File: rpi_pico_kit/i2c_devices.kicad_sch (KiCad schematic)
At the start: 6 parts, among them J10 OLED Display SSD1306, J11 Conn_01x04_Male, J12 Conn_01x04_Male, U8 AT24CS32

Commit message: changed footprints from 0805 to 0603
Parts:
- C28: footprint Capacitor_SMD:C_0805_2012Metric_Pad1.18x1.45mm_HandSolder -> Capacitor_SMD:C_0603_1608Metric_Pad1.08x0.95mm_HandSolder; Supplier Part URL https://www.digikey.cz/en/products/detail/kemet/C0805C104M3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 -> (none)
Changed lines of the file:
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@@
       (effects (font (size 1.27 1.27)))
     )
-    (property "Footprint" "Capacitor_SMD:C_0805_2012Metric_Pad1.18x1.45mm_HandSolder" (id 2) (at 231.14 82.8548 0)
+    (property "Footprint" "Capacitor_SMD:C_0603_1608Metric_Pad1.08x0.95mm_HandSolder" (id 2) (at 231.14 82.8548 0)
       (effects (font (size 1.27 1.27)) hide)
     )
@@
       (effects (font (size 1.27 1.27)) hide)
     )
-    (property "Supplier Part URL" "https://www.digikey.cz/en/products/detail/kemet/C0805C104M3RAC7800/2211748" (id 6) (at 227.33 83.82 0)
+    (property "Supplier Part URL" "" (id 6) (at 227.33 83.82 0)
       (effects (font (size 1.27 1.27)) hide)
     )

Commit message: changed footprints for resistor arrays
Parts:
- RN8: footprint Resistor_SMD:R_Array_Convex_4x1206 -> Resistor_SMD:R_Array_Convex_4x0603
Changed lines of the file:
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@@
       (effects (font (size 1.27 1.27)) (justify right))
     )
-    (property "Footprint" "Resistor_SMD:R_Array_Convex_4x1206" (id 2) (at 97.282 68.58 90)
+    (property "Footprint" "Resistor_SMD:R_Array_Convex_4x0603" (id 2) (at 97.282 68.58 90)
       (effects (font (size 1.27 1.27)) hide)
     )
@@
       (effects (font (size 1.27 1.27)) (justify right))
     )
-    (property "Footprint" "Resistor_SMD:R_Array_Convex_4x1206" (id 2) (at 59.182 68.58 90)
+    (property "Footprint" "Resistor_SMD:R_Array_Convex_4x0603" (id 2) (at 59.182 68.58 90)
       (effects (font (size 1.27 1.27)) hide)
     )
@@
       (effects (font (size 1.27 1.27)) (justify right))
     )
-    (property "Footprint" "Resistor_SMD:R_Array_Convex_4x1206" (id 2) (at 106.172 68.58 90)
+    (property "Footprint" "Resistor_SMD:R_Array_Convex_4x0603" (id 2) (at 106.172 68.58 90)
       (effects (font (size 1.27 1.27)) hide)
     )
@@
       (effects (font (size 1.27 1.27)) (justify right))
     )
-    (property "Footprint" "Resistor_SMD:R_Array_Convex_4x1206" (id 2) (at 68.072 68.58 90)
-      (effects (font (size 1.27 1.27)) hide)
-    )
+    (property "Footprint" "Resistor_SMD:R_Array_Convex_4x0603" (id 2) (at 68.072 68.58 90)
+      (effects (font (size 1.27 1.27)) hide)
+    )

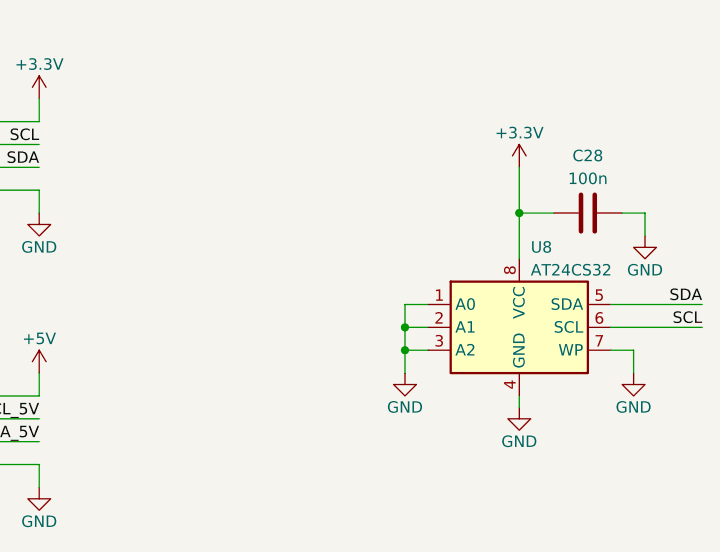
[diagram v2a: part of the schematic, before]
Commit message: changed eeprom I2C address from 0x50 to 0x51
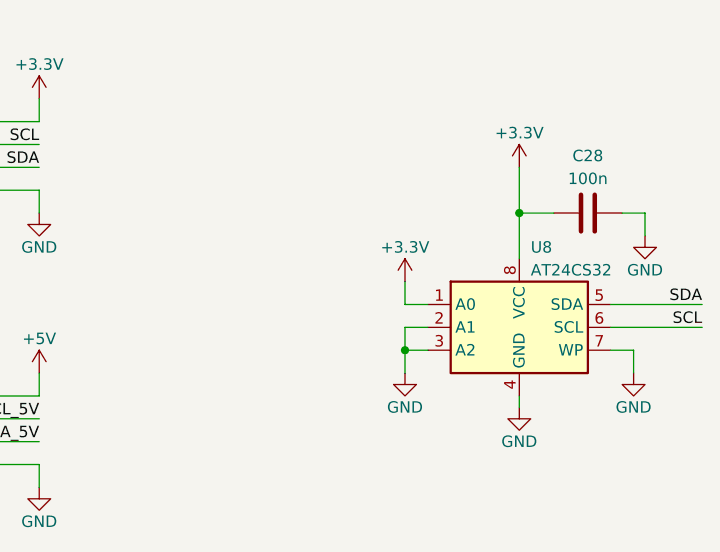
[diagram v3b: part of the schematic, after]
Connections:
- net +3V3: now also U8.1 (A0)
- net GND: no longer U8.1 (A0)
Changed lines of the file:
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@@
   (junction (at 219.71 83.82) (diameter 0) (color 0 0 0 0)
   )
-  (junction (at 207.01 96.52) (diameter 0) (color 0 0 0 0)
-  )
   (junction (at 104.14 80.01) (diameter 0) (color 0 0 0 0)
   )
@@
     (stroke (width 0) (type default))
   )
-  (wire (pts (xy 207.01 93.98) (xy 207.01 96.52))
-    (stroke (width 0) (type default))
-  )
   (wire (pts (xy 57.15 76.2) (xy 76.2 76.2))
     (stroke (width 0) (type default))
@@
     (stroke (width 0) (type default))
   )
+  (wire (pts (xy 229.87 96.52) (xy 240.03 96.52))
+    (stroke (width 0) (type default))
+  )
+  (wire (pts (xy 156.21 81.28) (xy 166.37 81.28))
+    (stroke (width 0) (type default))
+  )
   (wire (pts (xy 209.55 93.98) (xy 207.01 93.98))
     (stroke (width 0) (type default))
   )
-  (wire (pts (xy 229.87 96.52) (xy 240.03 96.52))
-    (stroke (width 0) (type default))
-  )
-  (wire (pts (xy 156.21 81.28) (xy 166.37 81.28))
-    (stroke (width 0) (type default))
-  )
   (wire (pts (xy 104.14 63.5) (xy 104.14 64.77))
     (stroke (width 0) (type default))
   )
   (wire (pts (xy 166.37 111.76) (xy 166.37 114.3))
+    (stroke (width 0) (type default))
+  )
+  (wire (pts (xy 207.01 93.98) (xy 207.01 91.44))
     (stroke (width 0) (type default))
   )
@@
     (pin "4")
   )
+  (symbol (lib_id "power:+3.3V") (at 207.01 91.44 0) (unit 1)
+    (in_bom yes) (on_board yes)
+    (property "Reference" "#PWR0155" (id 0) (at 207.01 95.25 0)
+      (effects (font (size 1.27 1.27)) hide)
+    )
+    (property "Value" "+3.3V" (id 1) (at 207.01 87.63 0)
+      (effects (font (size 1.27 1.27)))
+    )
+    (property "Footprint" "" (id 2) (at 207.01 91.44 0)
+      (effects (font (size 1.27 1.27)) hide)
+    )
+    (property "Datasheet" "" (id 3) (at 207.01 91.44 0)
+      (effects (font (size 1.27 1.27)) hide)
+    )
+    (pin "1")
+  )
   (symbol (lib_id "Memory_EEPROM:AT24CS32-SSHM") (at 219.71 96.52 0) (unit 1)

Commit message: i2c (unrouted 74)
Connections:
- net +3V3: now also RN8.2 (R2.1), RN8.4 (R4.1); no longer RN8.3 (R3.1), RN8.4 (R4.1)
- net +5V: now also RN8.1 (R1.1), RN8.3 (R3.1); no longer RN8.1 (R1.1), RN8.2 (R2.1)
- net SCL: now also RN8.5 (R4.2); no longer RN8.6 (R3.2)
- net SCL_5V: now also RN8.6 (R3.2); no longer RN8.8 (R1.2)
- net SDA: now also RN8.7 (R2.2); no longer RN8.5 (R4.2)
- net SDA_5V: now also RN8.8 (R1.2); no longer RN8.7 (R2.2)
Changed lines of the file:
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@@
     (pin "2")
   )
-  (symbol (lib_id "Device:R_Pack04_Split") (at 95.25 68.58 180) (unit 3)
+  (symbol (lib_id "Device:R_Pack04_Split") (at 95.25 68.58 180) (unit 4)
     (in_bom yes) (on_board yes)
     (property "Reference" "RN8" (id 0) (at 96.52 67.31 0)
@@
     )
     (property "Datasheet" "~" (id 3) (at 95.25 68.58 0)
+      (effects (font (size 1.27 1.27)) hide)
+    )
+    (pin "4")
+    (pin "5")
+  )
+  (symbol (lib_id "power:GND") (at 166.37 114.3 0) (unit 1)
+    (in_bom yes) (on_board yes)
+    (property "Reference" "#PWR0115" (id 0) (at 166.37 120.65 0)
+      (effects (font (size 1.27 1.27)) hide)
+    )
+    (property "Value" "GND" (id 1) (at 166.37 118.11 0)
+      (effects (font (size 1.27 1.27)))
+    )
+    (property "Footprint" "" (id 2) (at 166.37 114.3 0)
+      (effects (font (size 1.27 1.27)) hide)
+    )
+    (property "Datasheet" "" (id 3) (at 166.37 114.3 0)
+      (effects (font (size 1.27 1.27)) hide)
+    )
+    (pin "1")
+  )
+  (symbol (lib_id "Device:R_Pack04_Split") (at 57.15 68.58 180) (unit 3)
+    (in_bom yes) (on_board yes)
+    (property "Reference" "RN8" (id 0) (at 58.42 67.31 0)
+      (effects (font (size 1.27 1.27)) (justify right))
+    )
+    (property "Value" "4.7k" (id 1) (at 58.42 69.85 0)
+      (effects (font (size 1.27 1.27)) (justify right))
+    )
+    (property "Footprint" "Resistor_SMD:R_Array_Convex_4x0603" (id 2) (at 59.182 68.58 90)
+      (effects (font (size 1.27 1.27)) hide)
+    )
+    (property "Datasheet" "~" (id 3) (at 57.15 68.58 0)
       (effects (font (size 1.27 1.27)) hide)
     )
@@
     (pin "6")
   )
-  (symbol (lib_id "power:GND") (at 166.37 114.3 0) (unit 1)
-    (in_bom yes) (on_board yes)
-    (property "Reference" "#PWR0115" (id 0) (at 166.37 120.65 0)
-      (effects (font (size 1.27 1.27)) hide)
-    )
-    (property "Value" "GND" (id 1) (at 166.37 118.11 0)
-      (effects (font (size 1.27 1.27)))
-    )
-    (property "Footprint" "" (id 2) (at 166.37 114.3 0)
-      (effects (font (size 1.27 1.27)) hide)
-    )
-    (property "Datasheet" "" (id 3) (at 166.37 114.3 0)
-      (effects (font (size 1.27 1.27)) hide)
-    )
-    (pin "1")
-  )
-  (symbol (lib_id "Device:R_Pack04_Split") (at 57.15 68.58 180) (unit 1)
-    (in_bom yes) (on_board yes)
-    (property "Reference" "RN8" (id 0) (at 58.42 67.31 0)
-      (effects (font (size 1.27 1.27)) (justify right))
-    )
-    (property "Value" "4.7k" (id 1) (at 58.42 69.85 0)
-      (effects (font (size 1.27 1.27)) (justify right))
-    )
-    (property "Footprint" "Resistor_SMD:R_Array_Convex_4x0603" (id 2) (at 59.182 68.58 90)
-      (effects (font (size 1.27 1.27)) hide)
-    )
-    (property "Datasheet" "~" (id 3) (at 57.15 68.58 0)
-      (effects (font (size 1.27 1.27)) hide)
-    )
-    (pin "1")
-    (pin "8")
-  )
   (symbol (lib_id "power:+3.3V") (at 166.37 71.12 0) (unit 1)
     (in_bom yes) (on_board yes)
@@
     (pin "1")
   )
-  (symbol (lib_id "Device:R_Pack04_Split") (at 104.14 68.58 180) (unit 4)
+  (symbol (lib_id "Device:R_Pack04_Split") (at 104.14 68.58 180) (unit 2)
     (in_bom yes) (on_board yes)
     (property "Reference" "RN8" (id 0) (at 105.41 67.31 0)
@@
       (effects (font (size 1.27 1.27)) hide)
     )
-    (pin "4")
-    (pin "5")
+    (pin "2")
+    (pin "7")
   )
   (symbol (lib_id "power:GND") (at 232.41 101.6 0) (unit 1)
@@
     (pin "1")
   )
-  (symbol (lib_id "Device:R_Pack04_Split") (at 66.04 68.58 180) (unit 2)
+  (symbol (lib_id "Device:R_Pack04_Split") (at 66.04 68.58 180) (unit 1)
     (in_bom yes) (on_board yes)
     (property "Reference" "RN8" (id 0) (at 67.31 67.31 0)
@@
       (effects (font (size 1.27 1.27)) hide)
     )
-    (pin "2")
-    (pin "7")
+    (pin "1")
+    (pin "8")
   )
   (symbol (lib_id "Connector:Conn_01x04_Male") (at 151.13 106.68 0) (unit 1)

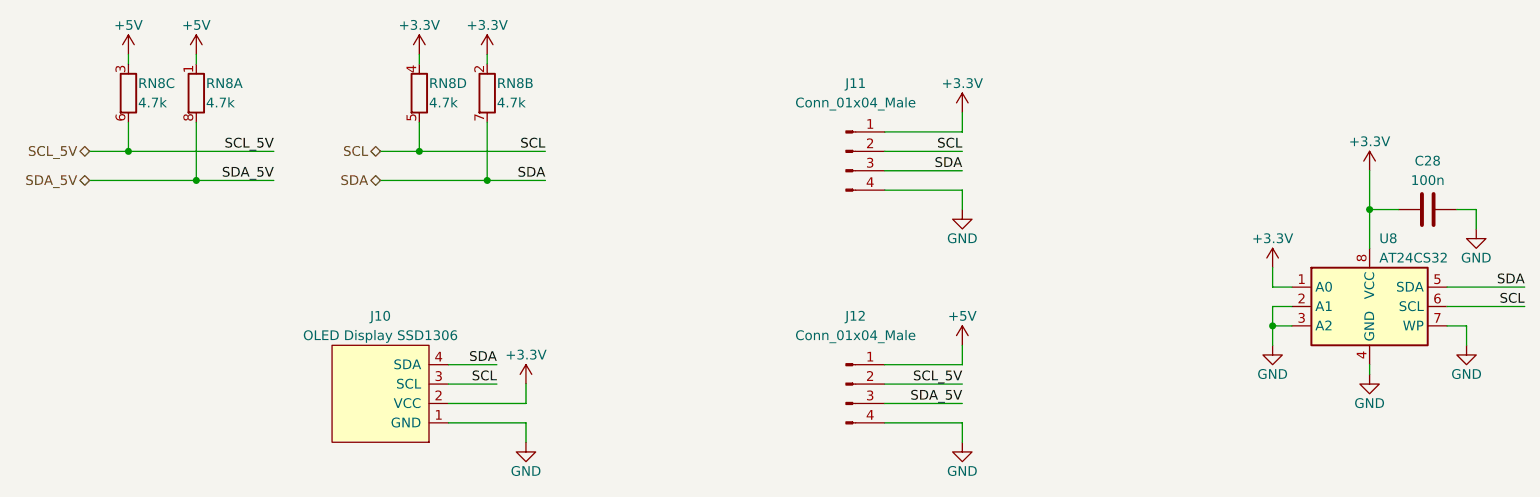
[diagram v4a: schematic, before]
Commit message: schematic cleared annotation
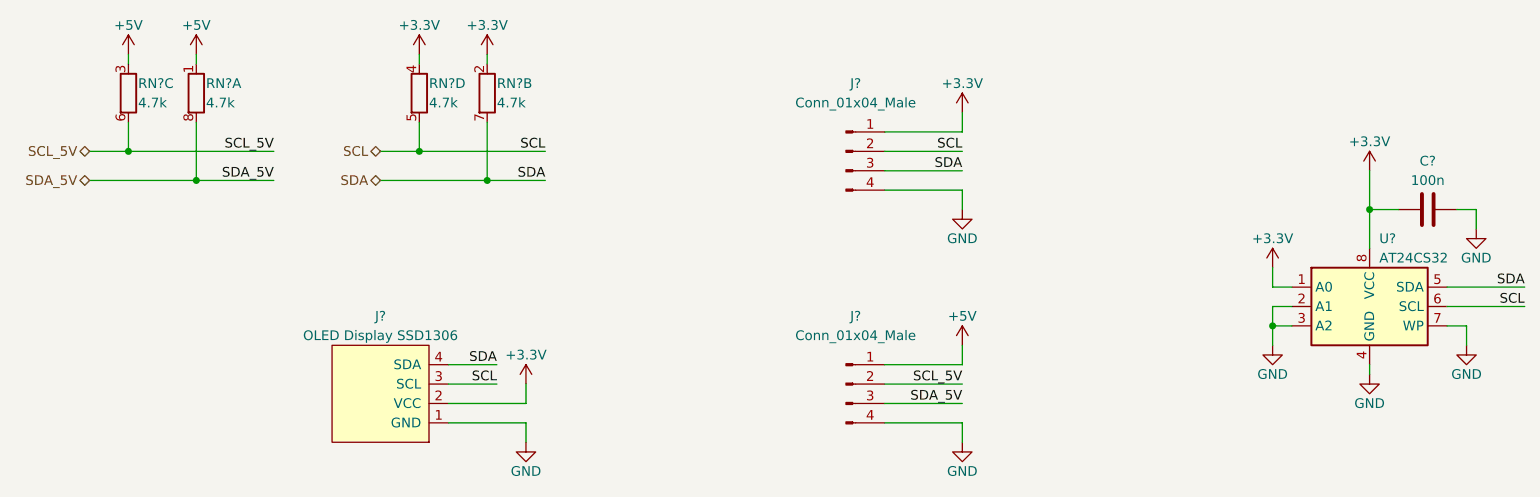
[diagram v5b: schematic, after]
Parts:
- renumbered C28 to C?, J10 to J?, J11 to J?, J12 to J?, RN8 to RN?, U8 to U?
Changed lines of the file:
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@@
   (symbol (lib_id "Device:C") (at 227.33 83.82 90) (unit 1)
     (in_bom yes) (on_board yes)
-    (property "Reference" "C28" (id 0) (at 227.33 77.47 90)
+    (property "Reference" "C?" (id 0) (at 227.33 77.47 90)
       (effects (font (size 1.27 1.27)))
     )
@@
   (symbol (lib_id "Device:R_Pack04_Split") (at 95.25 68.58 180) (unit 4)
     (in_bom yes) (on_board yes)
-    (property "Reference" "RN8" (id 0) (at 96.52 67.31 0)
+    (property "Reference" "RN?" (id 0) (at 96.52 67.31 0)
       (effects (font (size 1.27 1.27)) (justify right))
     )
@@
   (symbol (lib_id "power:GND") (at 166.37 114.3 0) (unit 1)
     (in_bom yes) (on_board yes)
-    (property "Reference" "#PWR0115" (id 0) (at 166.37 120.65 0)
+    (property "Reference" "#PWR?" (id 0) (at 166.37 120.65 0)
       (effects (font (size 1.27 1.27)) hide)
     )
@@
   (symbol (lib_id "Device:R_Pack04_Split") (at 57.15 68.58 180) (unit 3)
     (in_bom yes) (on_board yes)
-    (property "Reference" "RN8" (id 0) (at 58.42 67.31 0)
+    (property "Reference" "RN?" (id 0) (at 58.42 67.31 0)
       (effects (font (size 1.27 1.27)) (justify right))
     )
@@
   (symbol (lib_id "power:+3.3V") (at 166.37 71.12 0) (unit 1)
     (in_bom yes) (on_board yes)
-    (property "Reference" "#PWR0112" (id 0) (at 166.37 74.93 0)
+    (property "Reference" "#PWR?" (id 0) (at 166.37 74.93 0)
       (effects (font (size 1.27 1.27)) hide)
     )
@@
   (symbol (lib_id "power:GND") (at 166.37 83.82 0) (unit 1)
     (in_bom yes) (on_board yes)
-    (property "Reference" "#PWR0113" (id 0) (at 166.37 90.17 0)
+    (property "Reference" "#PWR?" (id 0) (at 166.37 90.17 0)
       (effects (font (size 1.27 1.27)) hide)
     )
@@
   (symbol (lib_id "power:GND") (at 109.22 114.3 0) (unit 1)
     (in_bom yes) (on_board yes)
-    (property "Reference" "#PWR0111" (id 0) (at 109.22 120.65 0)
+    (property "Reference" "#PWR?" (id 0) (at 109.22 120.65 0)
       (effects (font (size 1.27 1.27)) hide)
     )
@@
   (symbol (lib_id "Device:R_Pack04_Split") (at 104.14 68.58 180) (unit 2)
     (in_bom yes) (on_board yes)
-    (property "Reference" "RN8" (id 0) (at 105.41 67.31 0)
+    (property "Reference" "RN?" (id 0) (at 105.41 67.31 0)
       (effects (font (size 1.27 1.27)) (justify right))
     )
@@
   (symbol (lib_id "power:GND") (at 232.41 101.6 0) (unit 1)
     (in_bom yes) (on_board yes)
-    (property "Reference" "#PWR0119" (id 0) (at 232.41 107.95 0)
+    (property "Reference" "#PWR?" (id 0) (at 232.41 107.95 0)
       (effects (font (size 1.27 1.27)) hide)
     )
@@
   (symbol (lib_id "power:+5V") (at 57.15 63.5 0) (unit 1)
     (in_bom yes) (on_board yes)
-    (property "Reference" "#PWR0106" (id 0) (at 57.15 67.31 0)
+    (property "Reference" "#PWR?" (id 0) (at 57.15 67.31 0)
       (effects (font (size 1.27 1.27)) hide)
     )
@@
   (symbol (lib_id "power:+3.3V") (at 95.25 63.5 0) (unit 1)
     (in_bom yes) (on_board yes)
-    (property "Reference" "#PWR0108" (id 0) (at 95.25 67.31 0)
+    (property "Reference" "#PWR?" (id 0) (at 95.25 67.31 0)
       (effects (font (size 1.27 1.27)) hide)
     )
@@
   (symbol (lib_id "power:+3.3V") (at 104.14 63.5 0) (unit 1)
     (in_bom yes) (on_board yes)
-    (property "Reference" "#PWR0109" (id 0) (at 104.14 67.31 0)
+    (property "Reference" "#PWR?" (id 0) (at 104.14 67.31 0)
       (effects (font (size 1.27 1.27)) hide)
     )
@@
   (symbol (lib_id "SSD1306:SSD1306") (at 90.17 107.95 270) (mirror x) (unit 1)
     (in_bom yes) (on_board yes) (fields_autoplaced)
-    (property "Reference" "J10" (id 0) (at 90.17 97.79 90)
+    (property "Reference" "J?" (id 0) (at 90.17 97.79 90)
       (effects (font (size 1.27 1.27)))
     )
@@
   (symbol (lib_id "power:+3.3V") (at 207.01 91.44 0) (unit 1)
     (in_bom yes) (on_board yes)
-    (property "Reference" "#PWR0155" (id 0) (at 207.01 95.25 0)
+    (property "Reference" "#PWR?" (id 0) (at 207.01 95.25 0)
       (effects (font (size 1.27 1.27)) hide)
     )
@@
   (symbol (lib_id "Memory_EEPROM:AT24CS32-SSHM") (at 219.71 96.52 0) (unit 1)
     (in_bom yes) (on_board yes)
-    (property "Reference" "U8" (id 0) (at 220.98 87.63 0)
+    (property "Reference" "U?" (id 0) (at 220.98 87.63 0)
       (effects (font (size 1.27 1.27)) (justify left))
     )
@@
   (symbol (lib_id "Connector:Conn_01x04_Male") (at 151.13 76.2 0) (unit 1)
     (in_bom yes) (on_board yes)
-    (property "Reference" "J11" (id 0) (at 152.4 67.31 0)
+    (property "Reference" "J?" (id 0) (at 152.4 67.31 0)
       (effects (font (size 1.27 1.27)))
     )
@@
   (symbol (lib_id "power:+5V") (at 66.04 63.5 0) (unit 1)
     (in_bom yes) (on_board yes)
-    (property "Reference" "#PWR0107" (id 0) (at 66.04 67.31 0)
+    (property "Reference" "#PWR?" (id 0) (at 66.04 67.31 0)
       (effects (font (size 1.27 1.27)) hide)
     )
@@
   (symbol (lib_id "Device:R_Pack04_Split") (at 66.04 68.58 180) (unit 1)
     (in_bom yes) (on_board yes)
-    (property "Reference" "RN8" (id 0) (at 67.31 67.31 0)
+    (property "Reference" "RN?" (id 0) (at 67.31 67.31 0)
       (effects (font (size 1.27 1.27)) (justify right))
     )
@@
   (symbol (lib_id "Connector:Conn_01x04_Male") (at 151.13 106.68 0) (unit 1)
     (in_bom yes) (on_board yes)
-    (property "Reference" "J12" (id 0) (at 152.4 97.79 0)
+    (property "Reference" "J?" (id 0) (at 152.4 97.79 0)
       (effects (font (size 1.27 1.27)))
     )
@@
   (symbol (lib_id "power:+3.3V") (at 109.22 106.68 0) (unit 1)
     (in_bom yes) (on_board yes)
-    (property "Reference" "#PWR0110" (id 0) (at 109.22 110.49 0)
+    (property "Reference" "#PWR?" (id 0) (at 109.22 110.49 0)
       (effects (font (size 1.27 1.27)) hide)
     )
@@
   (symbol (lib_id "power:GND") (at 219.71 105.41 0) (unit 1)
     (in_bom yes) (on_board yes)
-    (property "Reference" "#PWR0118" (id 0) (at 219.71 111.76 0)
+    (property "Reference" "#PWR?" (id 0) (at 219.71 111.76 0)
       (effects (font (size 1.27 1.27)) hide)
     )
@@
   (symbol (lib_id "power:+5V") (at 166.37 101.6 0) (unit 1)
     (in_bom yes) (on_board yes)
-    (property "Reference" "#PWR0114" (id 0) (at 166.37 105.41 0)
+    (property "Reference" "#PWR?" (id 0) (at 166.37 105.41 0)
       (effects (font (size 1.27 1.27)) hide)
     )
@@
   (symbol (lib_id "power:GND") (at 207.01 101.6 0) (unit 1)
     (in_bom yes) (on_board yes)
-    (property "Reference" "#PWR0116" (id 0) (at 207.01 107.95 0)
+    (property "Reference" "#PWR?" (id 0) (at 207.01 107.95 0)
       (effects (font (size 1.27 1.27)) hide)
     )
@@
   (symbol (lib_id "power:+3.3V") (at 219.71 78.74 0) (unit 1)
     (in_bom yes) (on_board yes)
-    (property "Reference" "#PWR0117" (id 0) (at 219.71 82.55 0)
+    (property "Reference" "#PWR?" (id 0) (at 219.71 82.55 0)
       (effects (font (size 1.27 1.27)) hide)
     )
@@
   (symbol (lib_id "power:GND") (at 233.68 86.36 0) (unit 1)
     (in_bom yes) (on_board yes)
-    (property "Reference" "#PWR0120" (id 0) (at 233.68 92.71 0)
-      (effects (font (size 1.27 1.27)) hide)
-    )
+    (property "Reference" "#PWR?" (id 0) (at 233.68 92.71 0)
+      (effects (font (size 1.27 1.27)) hide)
+    )
